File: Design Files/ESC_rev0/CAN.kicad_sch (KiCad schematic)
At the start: 0 parts

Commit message: update 8
conclusion of mosfets and input protection; can almost concluded
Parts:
- added C45, C46: 10p, symbol Device:C
- added C47: 2u2, symbol Device:C
- added J7: Conn_01x04_Shielded, symbol Connector_Generic_Shielded:Conn_01x04_Shielded
- added L2: 744227S, WE-SL274, symbol 744227S:744227S
- added R40: 120R, symbol Device:R
- added R41, R42: 60R, symbol Device:R
- added R43: 10k, symbol Device:R
- added U5: ESDCAN24-2BLY, footprint:SOT-23-3_L3.0-W1.7-P0.95-LS2.9-BR, symbol ESDCAN24-2BLY:ESDCAN24-2BLY
- added U6: SN65HVD230, Package_SO:SOIC-8_3.9x4.9mm_P1.27mm, symbol Interface_CAN_LIN:SN65HVD230
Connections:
- new net: R43.1, U6.8 (Rs)
- new net +3V3: C47.1, U6.3 (VCC)
- new net +5V: J7.4 (Pin_4)
- new net CAN_N: L2.3 (4), U6.6 (CANL)
- new net CAN_P: L2.4 (2), U6.7 (CANH)
- new net CAN_RX: U6.4 (R)
- new net CAN_TX: U6.1 (D)
- new net C_CAN_N: C46.1, J7.2 (Pin_2), R40.2, R42.1, U5.2
- new net C_CAN_P: C45.2, J7.3 (Pin_3), R40.1, R41.1, U5.1
- new net GND: C45.1, C46.2, C47.2, J7.1 (Pin_1), R43.2, U5.3, U6.2 (GND)
- new net R_CAN_N: L2.2 (3), R42.2
- new net R_CAN_P: L2.1, R41.2
- no-connect marks 0 -> 2
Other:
- note added: "${TITLE}"
- note added: "Bypass Place as close as possible to the IC"
- note added: "Choke"
- note added: "Dark bold nets must be routed as differential pairs"
- note added: "Mode Selection Resistor 10k -> ~15 V/µs Slew Rate Check datasheet for more info"
- title: (none) -> CAN

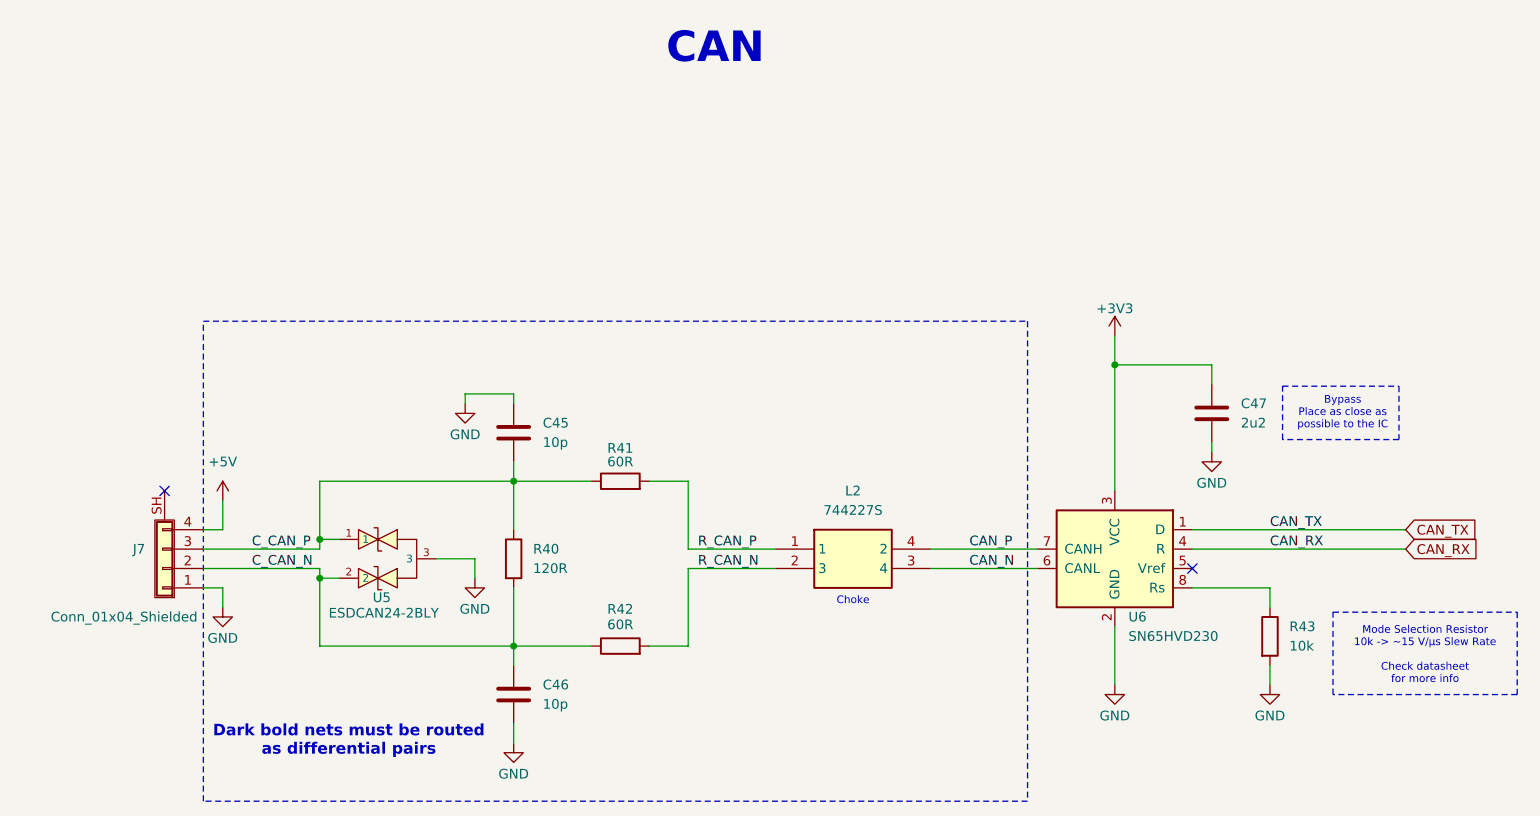
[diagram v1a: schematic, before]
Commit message: UPDATE 12
started schematics revision: edit and added info and circuits to some pages and assigned some footprints for components
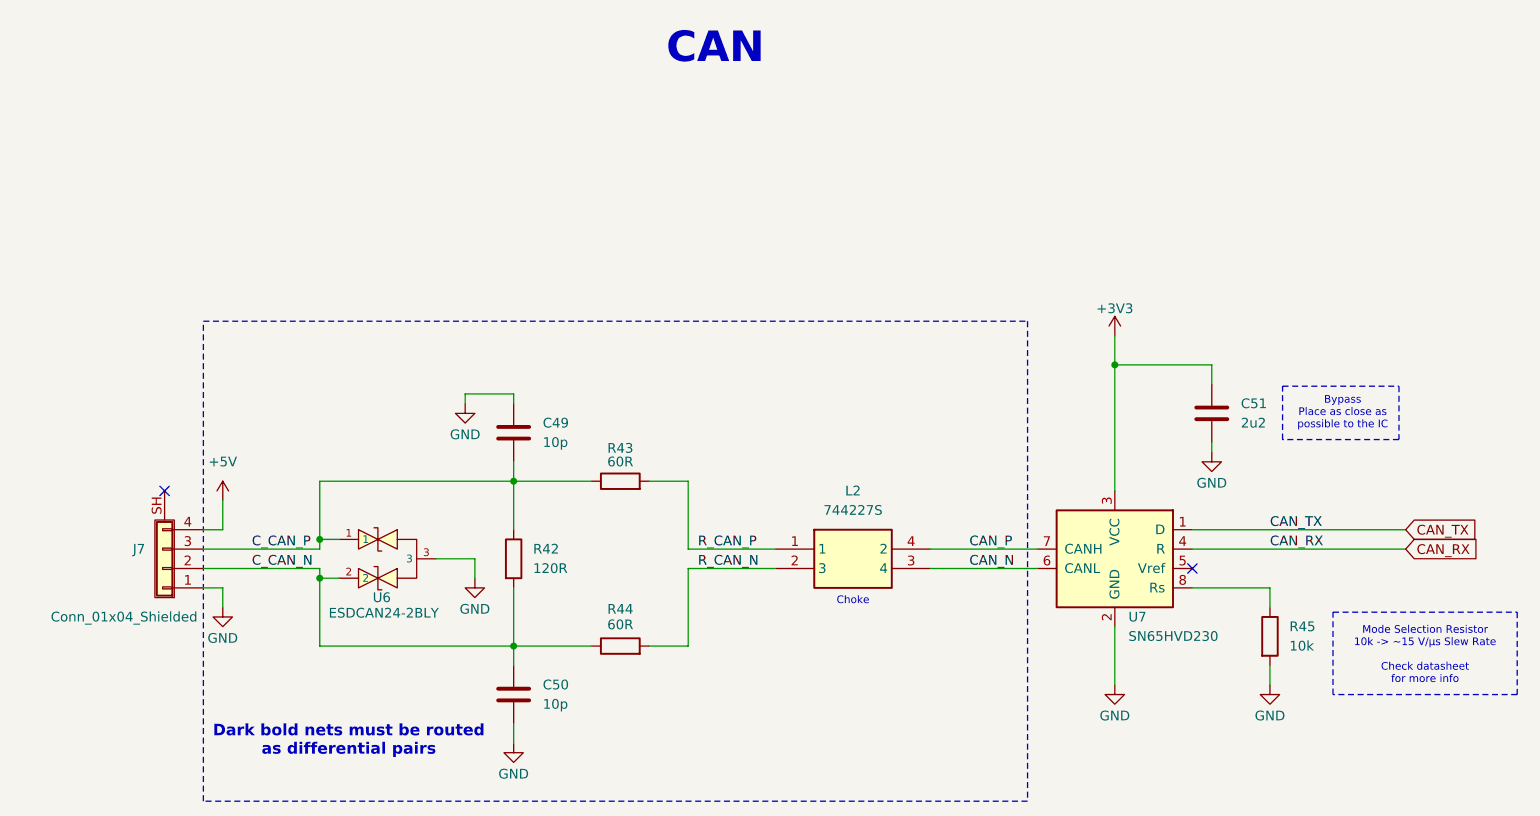
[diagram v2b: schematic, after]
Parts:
- C49: renamed from C45; footprint (none) -> Capacitor_SMD:C_0201_0603Metric
- C50: renamed from C46; footprint (none) -> Capacitor_SMD:C_0201_0603Metric
- C51: renamed from C47; footprint (none) -> Capacitor_SMD:C_0201_0603Metric
- L2: footprint WE-SL274 -> 744227S_foot:WE-SL274
- renumbered R40 to R42, R41 to R43, R42 to R44, R43 to R45, U5 to U6, U6 to U7
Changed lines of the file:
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@@
 		(on_board yes)
 		(dnp no)
-		(property "Reference" "#PWR058"
+		(property "Reference" "#PWR062"
 			(at 104.14 111.76 0)
 			(effects
@@
 			(project "ESC_rev0"
 				(path "/7906e740-34c4-4b06-b70f-1daa08872946/266b9186-051e-444d-b818-05c34306ea22"
-					(reference "#PWR058")
+					(reference "#PWR062")
 					(unit 1)
 				)
@@
 		(dnp no)
 		(fields_autoplaced yes)
-		(property "Reference" "C47"
+		(property "Reference" "C51"
 			(at 204.47 82.5499 0)
 			(effects
@@
 			)
 		)
-		(property "Footprint" ""
+		(property "Footprint" "Capacitor_SMD:C_0201_0603Metric"
 			(at 201.6252 87.63 0)
 			(effects
@@
 			(project ""
 				(path "/7906e740-34c4-4b06-b70f-1daa08872946/266b9186-051e-444d-b818-05c34306ea22"
-					(reference "C47")
+					(reference "C51")
 					(unit 1)
 				)
@@
 		(on_board yes)
 		(dnp no)
-		(property "Reference" "#PWR062"
+		(property "Reference" "#PWR064"
 			(at 187.96 77.47 0)
 			(effects
@@
 			(project ""
 				(path "/7906e740-34c4-4b06-b70f-1daa08872946/266b9186-051e-444d-b818-05c34306ea22"
-					(reference "#PWR062")
+					(reference "#PWR064")
 					(unit 1)
 				)
@@
 		(on_board yes)
 		(dnp no)
-		(property "Reference" "#PWR063"
+		(property "Reference" "#PWR066"
 			(at 200.66 95.25 0)
 			(effects
@@
 			(project "ESC_rev0"
 				(path "/7906e740-34c4-4b06-b70f-1daa08872946/266b9186-051e-444d-b818-05c34306ea22"
-					(reference "#PWR063")
+					(reference "#PWR066")
 					(unit 1)
 				)
@@
 		(on_board yes)
 		(dnp no)
-		(property "Reference" "R42"
+		(property "Reference" "R44"
 			(at 123.19 109.474 90)
 			(effects
@@
 			(project "ESC_rev0"
 				(path "/7906e740-34c4-4b06-b70f-1daa08872946/266b9186-051e-444d-b818-05c34306ea22"
-					(reference "R42")
+					(reference "R44")
 					(unit 1)
 				)
@@
 		(on_board yes)
 		(dnp no)
-		(property "Reference" "#PWR064"
+		(property "Reference" "#PWR067"
 			(at 208.28 125.73 0)
 			(effects
@@
 			(project "ESC_rev0"
 				(path "/7906e740-34c4-4b06-b70f-1daa08872946/266b9186-051e-444d-b818-05c34306ea22"
-					(reference "#PWR064")
+					(reference "#PWR067")
 					(unit 1)
 				)
@@
 		(dnp no)
 		(fields_autoplaced yes)
-		(property "Reference" "C45"
+		(property "Reference" "C49"
 			(at 113.03 85.0899 0)
 			(effects
@@
 			)
 		)
-		(property "Footprint" ""
+		(property "Footprint" "Capacitor_SMD:C_0201_0603Metric"
 			(at 110.1852 90.17 0)
 			(effects
@@
 			(project ""
 				(path "/7906e740-34c4-4b06-b70f-1daa08872946/266b9186-051e-444d-b818-05c34306ea22"
-					(reference "C45")
+					(reference "C49")
 					(unit 1)
 				)
@@
 		(dnp no)
 		(fields_autoplaced yes)
-		(property "Reference" "R40"
+		(property "Reference" "R42"
 			(at 111.76 101.5999 0)
 			(effects
@@
 			(project ""
 				(path "/7906e740-34c4-4b06-b70f-1daa08872946/266b9186-051e-444d-b818-05c34306ea22"
-					(reference "R40")
+					(reference "R42")
 					(unit 1)
 				)
@@
 		(on_board yes)
 		(dnp no)
-		(property "Reference" "#PWR060"
+		(property "Reference" "#PWR061"
 			(at 102.87 88.9 0)
 			(effects
@@
 			(project "ESC_rev0"
 				(path "/7906e740-34c4-4b06-b70f-1daa08872946/266b9186-051e-444d-b818-05c34306ea22"
-					(reference "#PWR060")
+					(reference "#PWR061")
 					(unit 1)
 				)
@@
 		(on_board yes)
 		(dnp no)
-		(property "Reference" "#PWR057"
+		(property "Reference" "#PWR060"
 			(at 71.12 115.57 0)
 			(effects
@@
 			(project ""
 				(path "/7906e740-34c4-4b06-b70f-1daa08872946/266b9186-051e-444d-b818-05c34306ea22"
-					(reference "#PWR057")
+					(reference "#PWR060")
 					(unit 1)
 				)
@@
 		(on_board yes)
 		(dnp no)
-		(property "Reference" "U5"
+		(property "Reference" "U6"
 			(at 91.948 107.95 90)
 			(effects
@@
 			(project ""
 				(path "/7906e740-34c4-4b06-b70f-1daa08872946/266b9186-051e-444d-b818-05c34306ea22"
-					(reference "U5")
+					(reference "U6")
 					(unit 1)
 				)
@@
 			)
 		)
-		(property "Footprint" "WE-SL274"
+		(property "Footprint" "744227S_foot:WE-SL274"
 			(at 160.02 196.52 0)
 			(effects
@@
 		(on_board yes)
 		(dnp no)
-		(property "Reference" "U6"
+		(property "Reference" "U7"
 			(at 189.738 110.49 0)
 			(effects
@@
 			(project ""
 				(path "/7906e740-34c4-4b06-b70f-1daa08872946/266b9186-051e-444d-b818-05c34306ea22"
-					(reference "U6")
+					(reference "U7")
 					(unit 1)
 				)
@@
 		(dnp no)
 		(fields_autoplaced yes)
-		(property "Reference" "#PWR056"
+		(property "Reference" "#PWR059"
 			(at 71.12 99.06 0)
 			(effects
@@
 			(project ""
 				(path "/7906e740-34c4-4b06-b70f-1daa08872946/266b9186-051e-444d-b818-05c34306ea22"
-					(reference "#PWR056")
+					(reference "#PWR059")
 					(unit 1)
 				)
@@
 		(dnp no)
 		(fields_autoplaced yes)
-		(property "Reference" "C46"
+		(property "Reference" "C50"
 			(at 113.03 119.3799 0)
 			(effects
@@
 			)
 		)
-		(property "Footprint" ""
+		(property "Footprint" "Capacitor_SMD:C_0201_0603Metric"
 			(at 110.1852 124.46 0)
 			(effects
@@
 			(project "ESC_rev0"
 				(path "/7906e740-34c4-4b06-b70f-1daa08872946/266b9186-051e-444d-b818-05c34306ea22"
-					(reference "C46")
+					(reference "C50")
 					(unit 1)
 				)
@@
 		(on_board yes)
 		(dnp no)
-		(property "Reference" "#PWR061"
+		(property "Reference" "#PWR065"
 			(at 187.96 125.73 0)
 			(effects
@@
 			(project "ESC_rev0"
 				(path "/7906e740-34c4-4b06-b70f-1daa08872946/266b9186-051e-444d-b818-05c34306ea22"
-					(reference "#PWR061")
+					(reference "#PWR065")
 					(unit 1)
 				)
@@
 		(dnp no)
 		(fields_autoplaced yes)
-		(property "Reference" "R43"
+		(property "Reference" "R45"
 			(at 210.82 111.7599 0)
 			(effects
@@
 			(project ""
 				(path "/7906e740-34c4-4b06-b70f-1daa08872946/266b9186-051e-444d-b818-05c34306ea22"
-					(reference "R43")
+					(reference "R45")
 					(unit 1)
 				)
@@
 		(on_board yes)
 		(dnp no)
-		(property "Reference" "#PWR059"
+		(property "Reference" "#PWR063"
 			(at 109.22 133.35 0)
 			(effects
@@
 			(project "ESC_rev0"
 				(path "/7906e740-34c4-4b06-b70f-1daa08872946/266b9186-051e-444d-b818-05c34306ea22"
-					(reference "#PWR059")
+					(reference "#PWR063")
 					(unit 1)
 				)
@@
 		(on_board yes)
 		(dnp no)
-		(property "Reference" "R41"
+		(property "Reference" "R43"
 			(at 123.19 88.392 90)
 			(effects
@@
 			(project "ESC_rev0"
 				(path "/7906e740-34c4-4b06-b70f-1daa08872946/266b9186-051e-444d-b818-05c34306ea22"
-					(reference "R41")
-					(unit 1)
-				)
+					(reference "R43")
+					(unit 1)
+				)

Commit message: update 13
assigned all footprints (provisionally) and imported them - errors and warning occurred, must be corrected in the future
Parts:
- J7: footprint (none) -> Connector_PinHeader_2.00mm:PinHeader_1x04_P2.00mm_Vertical
- R42, R43, R44, R45: footprint (none) -> Resistor_SMD:R_0603_1608Metric
- U6: footprint footprint:SOT-23-3_L3.0-W1.7-P0.95-LS2.9-BR -> ESDCAN24-2BLY_ST_foot:SOT-23-3_L3.0-W1.7-P0.95-LS2.9-BR
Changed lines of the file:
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@@
 			)
 		)
-		(property "Footprint" ""
+		(property "Footprint" "Resistor_SMD:R_0603_1608Metric"
 			(at 123.19 116.078 90)
 			(effects
@@
 			)
 		)
-		(property "Footprint" ""
+		(property "Footprint" "Resistor_SMD:R_0603_1608Metric"
 			(at 107.442 102.87 90)
 			(effects
@@
 			)
 		)
-		(property "Footprint" ""
+		(property "Footprint" "Connector_PinHeader_2.00mm:PinHeader_1x04_P2.00mm_Vertical"
 			(at 63.5 104.14 0)
 			(effects
@@
 			)
 		)
-		(property "Footprint" "footprint:SOT-23-3_L3.0-W1.7-P0.95-LS2.9-BR"
+		(property "Footprint" "ESDCAN24-2BLY_ST_foot:SOT-23-3_L3.0-W1.7-P0.95-LS2.9-BR"
 			(at 81.28 102.87 0)
 			(effects
@@
 			)
 		)
-		(property "Footprint" ""
+		(property "Footprint" "Resistor_SMD:R_0603_1608Metric"
 			(at 206.502 113.03 90)
 			(effects
@@
 			)
 		)
-		(property "Footprint" ""
+		(property "Footprint" "Resistor_SMD:R_0603_1608Metric"
 			(at 123.19 94.488 90)
 			(effects

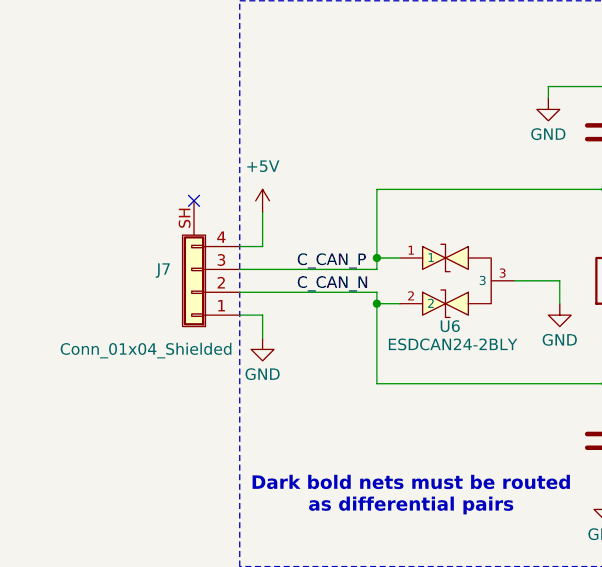
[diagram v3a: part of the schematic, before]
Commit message: update 15
Simple connectors replaced by smd connectors (downloaded). Connectors were placed in edges of the board.
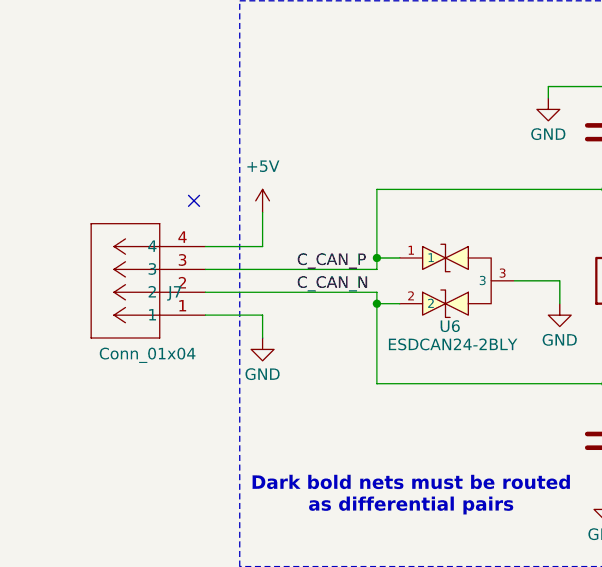
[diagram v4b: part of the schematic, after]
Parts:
- J7: value Conn_01x04_Shielded -> Conn_01x04; footprint Connector_PinHeader_2.00mm:PinHeader_1x04_P2.00mm_Vertical -> S4B-XH-SM4-TB:CONN4_S4B-XH_JST; symbol Connector_Generic_Shielded:Conn_01x04_Shielded -> S4B_XH_SM4_TB:S4B-XH-SM4-TB
- L2: footprint 744227S_foot:WE-SL274 -> WE-SL274
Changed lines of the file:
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@@
-	(wire
-		(pts
-			(xy 83.82 104.14) (xy 68.58 104.14)
-		)
-		(stroke
-			(width 0.5)
-			(type default)
-			(color 51 104 10 1)
-		)
-	)
 	(wire
 		(pts
@@
 	(wire
 		(pts
-			(xy 68.58 99.06) (xy 71.12 99.06)
-		)
-		(stroke
-			(width 0)
-			(type default)
-		)
-	)
-	(wire
-		(pts
 			(xy 83.82 105.41) (xy 83.82 104.14)
 		)
@@
 	(wire
 		(pts
-			(xy 68.58 106.68) (xy 71.12 106.68)
-		)
-		(stroke
-			(width 0)
-			(type default)
-		)
-	)
-	(wire
-		(pts
 			(xy 83.82 100.33) (xy 86.36 100.33)
 		)
@@
 	(wire
 		(pts
-			(xy 68.58 101.6) (xy 83.82 101.6)
-		)
-		(stroke
-			(width 0.5)
-			(type default)
-			(color 51 104 10 1)
+			(xy 64.77 99.06) (xy 71.12 99.06)
+		)
+		(stroke
+			(width 0)
+			(type default)
 		)
 	)
@@
 	(wire
 		(pts
+			(xy 64.77 106.68) (xy 71.12 106.68)
+		)
+		(stroke
+			(width 0)
+			(type default)
+		)
+	)
+	(wire
+		(pts
 			(xy 109.22 92.71) (xy 119.38 92.71)
 		)
@@
 	(wire
 		(pts
+			(xy 64.77 104.14) (xy 83.82 104.14)
+		)
+		(stroke
+			(width 0.5)
+			(type default)
+			(color 51 104 10 1)
+		)
+	)
+	(wire
+		(pts
 			(xy 198.12 99.06) (xy 226.06 99.06)
 		)
@@
 			(width 0)
 			(type default)
+		)
+	)
+	(wire
+		(pts
+			(xy 64.77 101.6) (xy 83.82 101.6)
+		)
+		(stroke
+			(width 0.5)
+			(type default)
+			(color 51 104 10 1)
 		)
 	)
@@
 	)
 	(symbol
-		(lib_id "Connector_Generic_Shielded:Conn_01x04_Shielded")
-		(at 63.5 104.14 180)
+		(lib_id "S4B_XH_SM4_TB:S4B-XH-SM4-TB")
+		(at 64.77 106.68 180)
 		(unit 1)
 		(exclude_from_sim no)
@@
 		(dnp no)
 		(property "Reference" "J7"
-			(at 60.96 101.5999 0)
+			(at 62.23 104.1399 0)
 			(effects
 				(font
@@
 			)
 		)
-		(property "Value" "Conn_01x04_Shielded"
-			(at 67.818 110.49 0)
+		(property "Value" "Conn_01x04"
+			(at 63.754 110.998 0)
 			(effects
 				(font
@@
 			)
 		)
-		(property "Footprint" "Connector_PinHeader_2.00mm:PinHeader_1x04_P2.00mm_Vertical"
-			(at 63.5 104.14 0)
-			(effects
-				(font
-					(size 1.27 1.27)
-				)
-				(hide yes)
-			)
-		)
-		(property "Datasheet" "~"
-			(at 63.5 104.14 0)
-			(effects
-				(font
-					(size 1.27 1.27)
+		(property "Footprint" "S4B-XH-SM4-TB:CONN4_S4B-XH_JST"
+			(at 64.77 106.68 0)
+			(effects
+				(font
+					(size 1.27 1.27)
+					(italic yes)
+				)
+				(hide yes)
+			)
+		)
+		(property "Datasheet" "S4B-XH-SM4-TB"
+			(at 64.77 106.68 0)
+			(effects
+				(font
+					(size 1.27 1.27)
+					(italic yes)
 				)
 				(hide yes)
@@
 		)
 		(property "Description" "Generic shielded connector, single row, 01x04, script generated (kicad-library-utils/schlib/autogen/connector/)"
-			(at 63.5 104.14 0)
+			(at 64.77 106.68 0)
 			(effects
 				(font
@@
 		)
 		(pin "4"
-		)
-		(pin "SH"
 		)
 		(instances
@@
 			)
 		)
-		(property "Footprint" "744227S_foot:WE-SL274"
+		(property "Footprint" "WE-SL274"
 			(at 160.02 196.52 0)
 			(effects
